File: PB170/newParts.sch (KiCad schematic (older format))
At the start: 4 parts, among them U2 74HC08, U3 74HC4511D, U4 HEF4518BT, U5 74HC32

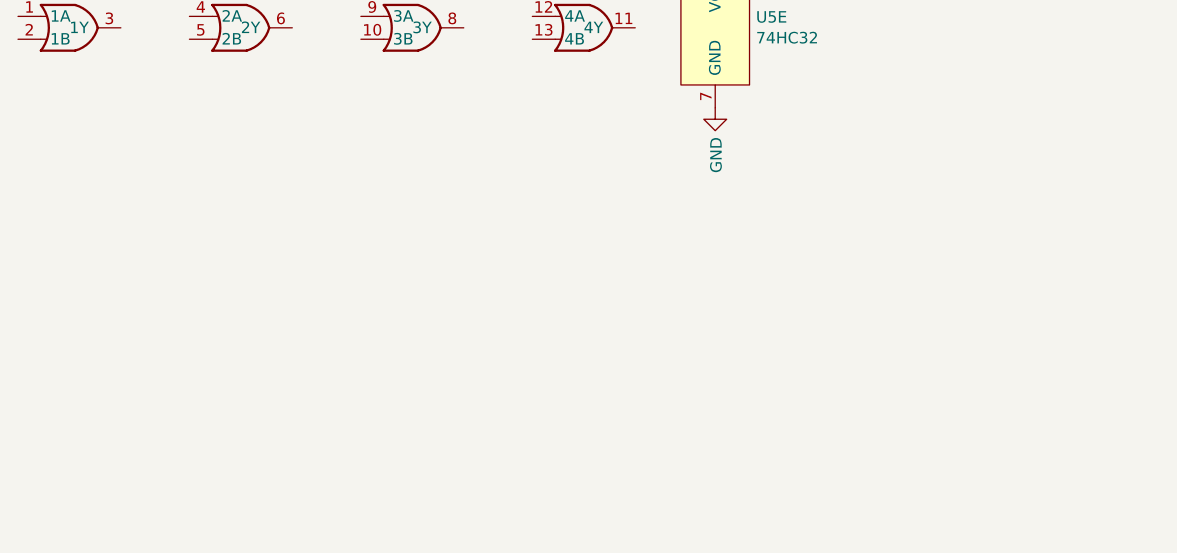
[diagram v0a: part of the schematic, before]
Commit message: Setup xor component, create ALU and ADDER sheets
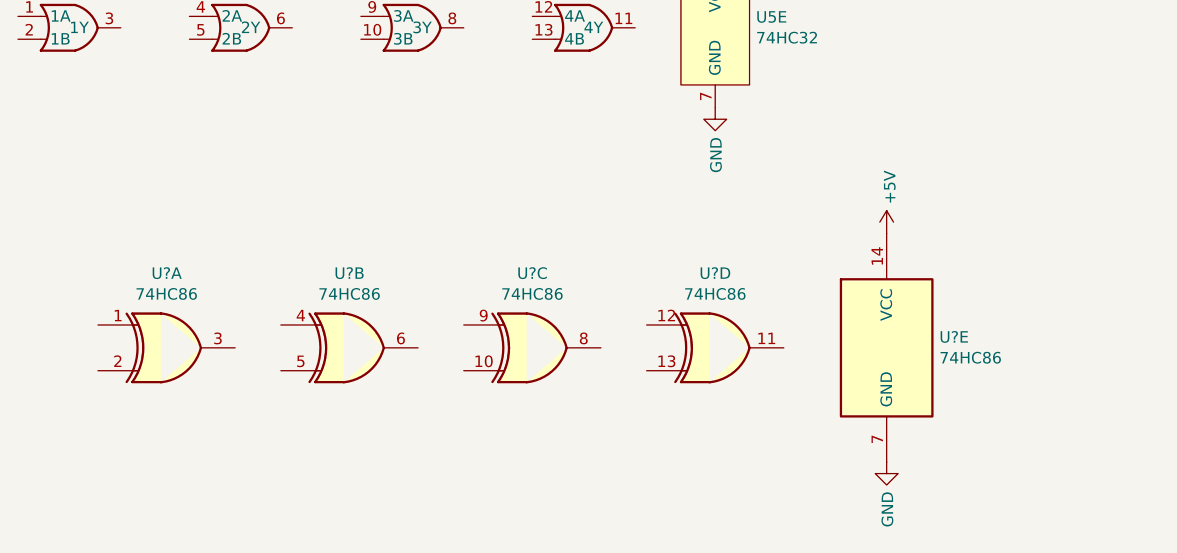
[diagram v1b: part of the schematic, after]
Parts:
- added U? (x5): 74HC86, Package_SO:TSSOP-14_4.4x5mm_P0.65mm, symbol 74xx:74HC86
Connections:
- net +5V: now also U?.14 (VCC)
- net GND: now also U?.7 (GND)
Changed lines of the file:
@@
 $Descr A4 11693 8268
 encoding utf-8
-Sheet 3 3
+Sheet 3 5
 Title ""
 Date ""
@@
 	1    0    0    -1
 $EndComp
+$Comp
+L 74xx:74HC86 U?
+U 1 1 600A8380
+P 1400 4200
+F 0 "U?" H 1400 4525 50  0000 C CNN
+F 1 "74HC86" H 1400 4434 50  0000 C CNN
+F 2 "Package_SO:TSSOP-14_4.4x5mm_P0.65mm" H 1400 4200 50  0001 C CNN
+F 3 "https://datasheet.lcsc.com/szlcsc/Texas-Instruments-TI-SN74AHC86PWR_C117522.pdf" H 1400 4200 50  0001 C CNN
+F 4 "C117522" H 1400 4200 50  0001 C CNN "LCSC"
+	1    1400 4200
+	1    0    0    -1
+$EndComp
+$Comp
+L 74xx:74HC86 U?
+U 2 1 600AA188
+P 2200 4200
+F 0 "U?" H 2200 4525 50  0000 C CNN
+F 1 "74HC86" H 2200 4434 50  0000 C CNN
+F 2 "Package_SO:TSSOP-14_4.4x5mm_P0.65mm" H 2200 4200 50  0001 C CNN
+F 3 "https://datasheet.lcsc.com/szlcsc/Texas-Instruments-TI-SN74AHC86PWR_C117522.pdf" H 2200 4200 50  0001 C CNN
+F 4 "C117522" H 2200 4200 50  0001 C CNN "LCSC"
+	2    2200 4200
+	1    0    0    -1
+$EndComp
+$Comp
+L 74xx:74HC86 U?
+U 3 1 600AF551
+P 3000 4200
+F 0 "U?" H 3000 4525 50  0000 C CNN
+F 1 "74HC86" H 3000 4434 50  0000 C CNN
+F 2 "Package_SO:TSSOP-14_4.4x5mm_P0.65mm" H 3000 4200 50  0001 C CNN
+F 3 "https://datasheet.lcsc.com/szlcsc/Texas-Instruments-TI-SN74AHC86PWR_C117522.pdf" H 3000 4200 50  0001 C CNN
+F 4 "C117522" H 3000 4200 50  0001 C CNN "LCSC"
+	3    3000 4200
+	1    0    0    -1
+$EndComp
+$Comp
+L 74xx:74HC86 U?
+U 4 1 600B0ABE
+P 3800 4200
+F 0 "U?" H 3800 4525 50  0000 C CNN
+F 1 "74HC86" H 3800 4434 50  0000 C CNN
+F 2 "Package_SO:TSSOP-14_4.4x5mm_P0.65mm" H 3800 4200 50  0001 C CNN
+F 3 "https://datasheet.lcsc.com/szlcsc/Texas-Instruments-TI-SN74AHC86PWR_C117522.pdf" H 3800 4200 50  0001 C CNN
+F 4 "C117522" H 3800 4200 50  0001 C CNN "LCSC"
+	4    3800 4200
+	1    0    0    -1
+$EndComp
+$Comp
+L 74xx:74HC86 U?
+U 5 1 600B2251
+P 4550 4200
+F 0 "U?" H 4780 4246 50  0000 L CNN
+F 1 "74HC86" H 4780 4155 50  0000 L CNN
+F 2 "Package_SO:TSSOP-14_4.4x5mm_P0.65mm" H 4550 4200 50  0001 C CNN
+F 3 "https://datasheet.lcsc.com/szlcsc/Texas-Instruments-TI-SN74AHC86PWR_C117522.pdf" H 4550 4200 50  0001 C CNN
+F 4 "C117522" H 4550 4200 50  0001 C CNN "LCSC"
+	5    4550 4200
+	1    0    0    -1
+$EndComp
+$Comp
+L power:+5V #PWR?
+U 1 1 600B6A3F
+P 4550 3700
+AR Path="/600B6A3F" Ref="#PWR?"  Part="1"
+AR Path="/5FEB4D4D/600B6A3F" Ref="#PWR?"  Part="1"
+F 0 "#PWR?" H 4550 3550 50  0001 C CNN
+F 1 "+5V" V 4565 3828 50  0000 L CNN
+F 2 "" H 4550 3700 50  0001 C CNN
+F 3 "" H 4550 3700 50  0001 C CNN
+	1    4550 3700
+	1    0    0    -1
+$EndComp
+$Comp
+L power:GND #PWR?
+U 1 1 600B7A17
+P 4550 4700
+AR Path="/600B7A17" Ref="#PWR?"  Part="1"
+AR Path="/5FEB4D4D/600B7A17" Ref="#PWR?"  Part="1"
+F 0 "#PWR?" H 4550 4450 50  0001 C CNN
+F 1 "GND" V 4555 4572 50  0000 R CNN
+F 2 "" H 4550 4700 50  0001 C CNN
+F 3 "" H 4550 4700 50  0001 C CNN
+	1    4550 4700
+	1    0    0    -1
+$EndComp
